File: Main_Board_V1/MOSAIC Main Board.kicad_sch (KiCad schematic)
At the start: 82 parts, among them J1 CONN E, J10 Right Angle Qwiic Connector, J11 Vertical Qwiic Connector, J12 CONN E, J13 CONN E, J14 35RAPC4BH3 CONN 3.5MM, J2 CONN E, J3 CONN E, J4 CONN HEADER VERT 10POS 1.27MM, J5 USB TYPE C R/A SMT 16PIN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

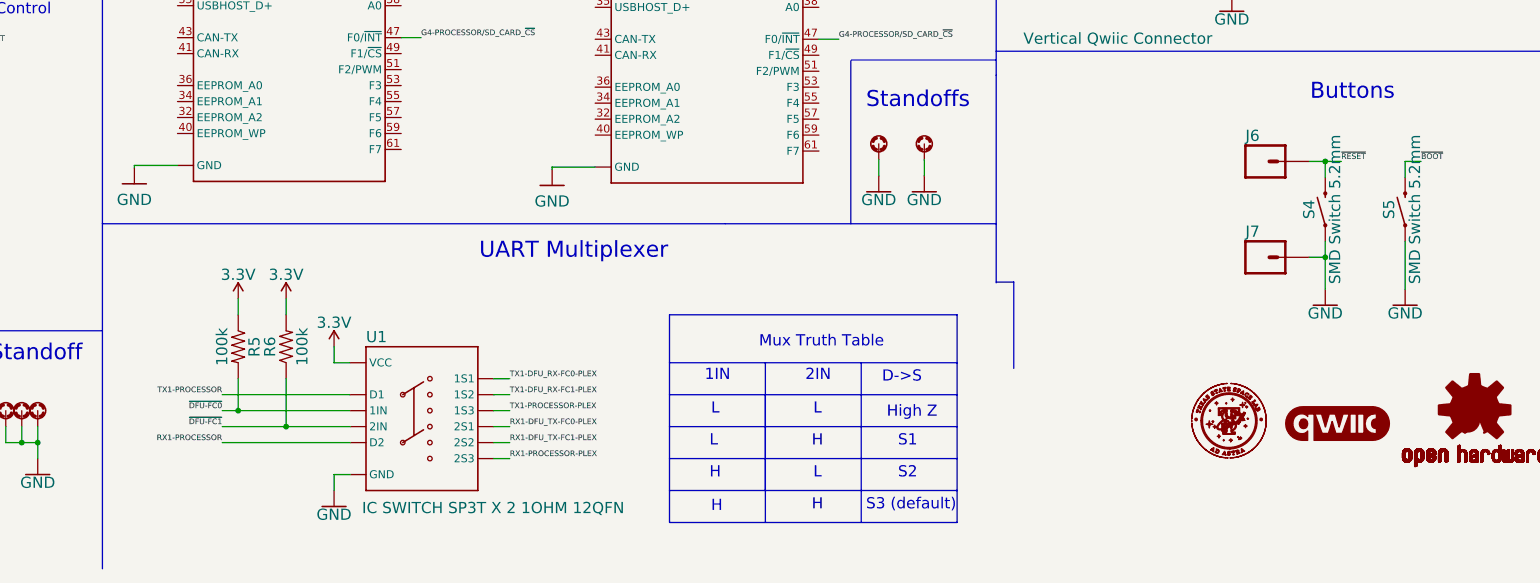
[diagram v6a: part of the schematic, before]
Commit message: finished comp sourcing
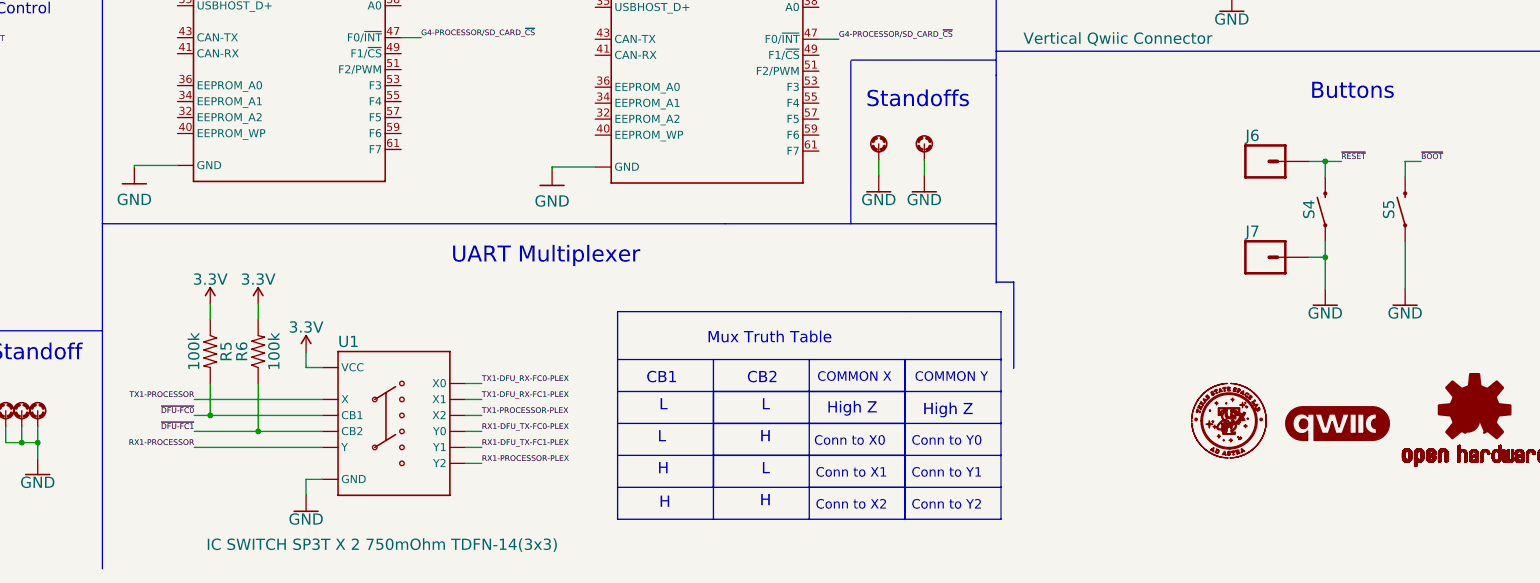
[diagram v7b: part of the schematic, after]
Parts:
- J6, J7: now left out of the parts list
- S4, S5: JLCPCB Part # (none) -> C10852; Source https://www.sparkfun.com/products/8720 -> (none)
- U1: value IC SWITCH SP3T X 2 1OHM 12QFN -> IC SWITCH SP3T X 2 750mOhm TDFN-14(3x3); footprint main_board_footprints_V1.0:STG3856 -> main_board_footprints_V1.0:TDFN-14-1EP_3x3mm_P0.4mm_EP1.78x2.35mm; symbol main_board_symbols_V1.0:STG3856QTR -> main_board_symbols_V1.0:MAX4932ETD+T; JLCPCB Part # (none) -> C1522710; Source https://www.digikey.com/en/products/detail/stmicroelectroni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 -> (none)
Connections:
- net 3.3V: now also U1.1 (VCC); no longer U1.P11 (VCC)
- net GND: now also U1.8 (GND); no longer U1.P5 (GND)
- net RX1-DFU_TX-FC0-PLEX: now also U1.9 (Y0); no longer U1.P9 (2S1)
- net RX1-DFU_TX-FC1-PLEX: now also U1.11 (Y1); no longer U1.P8 (2S2)
- net RX1-PROCESSOR: now also U1.14 (Y); no longer U1.P6 (D2)
- net RX1-PROCESSOR-PLEX: now also U1.12 (Y2); no longer U1.P7 (2S3)
- net TX1-DFU_RX-FC0-PLEX: now also U1.7 (X0); no longer U1.P1 (1S1)
- net TX1-DFU_RX-FC1-PLEX: now also U1.5 (X1); no longer U1.P2 (1S2)
- net TX1-PROCESSOR: now also U1.2 (X); no longer U1.P4 (D1)
- net TX1-PROCESSOR-PLEX: now also U1.4 (X2); no longer U1.P3 (1S3)
- net ~{DFU-FC0}: now also U1.6 (CB1); no longer U1.P12 (1IN)
- net ~{DFU-FC1}: now also U1.13 (CB2); no longer U1.P10 (2IN)
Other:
- note added: "CB1"
- note added: "CB2"
- note added: "COMMON X"
- note added: "COMMON Y"
- note added: "Conn to X0"
- note added: "Conn to X1"
- note added: "Conn to X2"
- note added: "Conn to Y0"
- note added: "Conn to Y1"
- note added: "Conn to Y2"
- note removed: "1IN"
- note removed: "2IN"
- note removed: "D->S"
- note removed: "S1"
- note removed: "S2"
- note removed: "S3 (default)"
- moved on the sheet: R5, R6, U1

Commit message: Finish comp placement
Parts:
- C3: footprint SparkFun_Main_Board_Double_v22:0603 -> main_board_footprints_V1.0:0805
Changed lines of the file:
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@@
 			)
 		)
-		(property "Footprint" "SparkFun_Main_Board_Double_v22:0603"
+		(property "Footprint" "main_board_footprints_V1.0:0805"
 			(at 352.298 69.088 0)
 			(effects
